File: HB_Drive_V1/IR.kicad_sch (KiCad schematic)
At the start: 55 parts, among them J1 Conn_02x05_Counter_Clockwise, J2 Conn_02x03_Counter_Clockwise, J3 Conn_01x02, U1 TL082, U13 TL082, U2 TL082, U3 TL082, U4 TL082

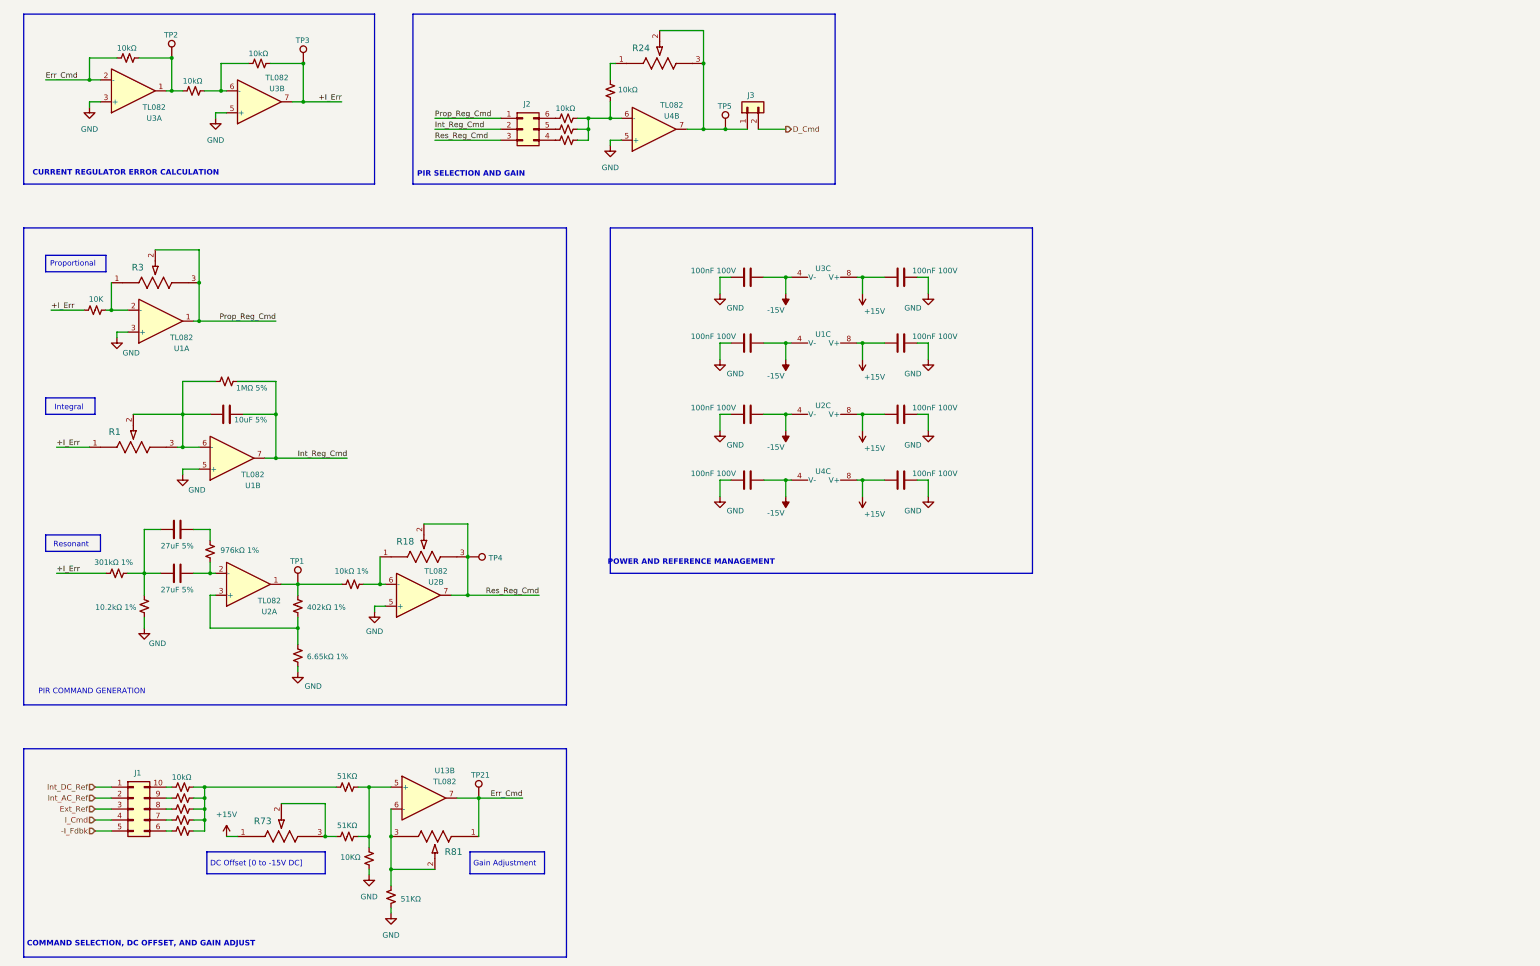
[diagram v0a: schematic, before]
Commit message: finishes hirearchical labels, add 10v +- ref generation and updates the DC offset circuits
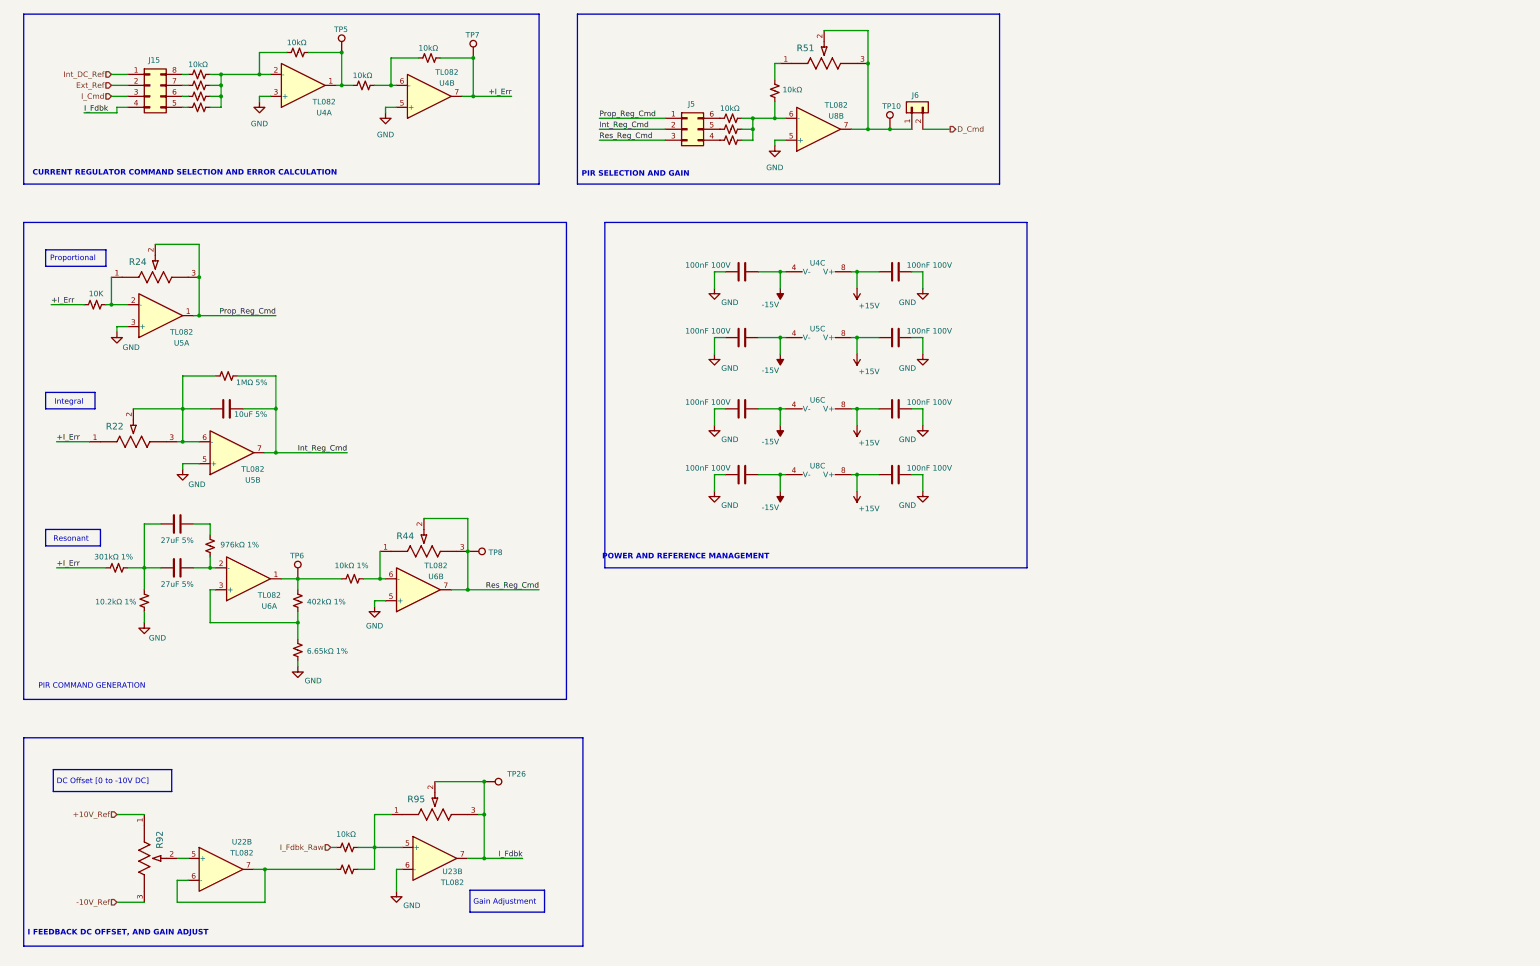
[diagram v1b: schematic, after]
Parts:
- removed J1: Conn_02x05_Counter_Clockwise, Connector_PinHeader_1.27mm:PinHeader_2x05_P1.27mm_Vertical, symbol Connector_Generic:Conn_02x05_Counter_Clockwise
- removed R10, R7, R8, R9: 10K, Resistor_SMD:R_0603_1608Metric_Pad0.98x0.95mm_HandSolder, symbol Device:R_Small_US
- removed R6: 10kΩ, Resistor_SMD:R_0603_1608Metric_Pad0.98x0.95mm_HandSolder, symbol Device:R_Small_US
- removed R73, R81: PV36W104C01B00, PV36W104C01B00:POT_PV36W_BRN, symbol PV36W104C01B00:PV36W104C01B00
- removed R74, R78, R80: 51KΩ, Resistor_SMD:R_0603_1608Metric_Pad0.98x0.95mm_HandSolder, symbol Device:R_Small_US
- removed R79: 10KΩ, Resistor_SMD:R_0603_1608Metric_Pad0.98x0.95mm_HandSolder, symbol Device:R_Small_US
- removed TP21: TestPoint, TestPoint:TestPoint_Loop_D2.60mm_Drill1.6mm_Beaded, symbol Connector:TestPoint
- removed U13: TL082, Package_SO:SOIC-8_5.3x5.3mm_P1.27mm, symbol Amplifier_Operational:TL082
- added J15: Conn_02x04_Counter_Clockwise, Connector_PinSocket_1.27mm:PinSocket_2x04_P1.27mm_Vertical, symbol Connector_Generic:Conn_02x04_Counter_Clockwise
- added R28, R93: 10kΩ, Resistor_SMD:R_0603_1608Metric_Pad0.98x0.95mm_HandSolder, symbol Device:R_Small_US
- added R29, R30, R31: 10K, Resistor_SMD:R_0603_1608Metric_Pad0.98x0.95mm_HandSolder, symbol Device:R_Small_US
- added R92: PV36W104C01B00, PV36W104C01B00:POT_PV36W_BRN, symbol PV36W104C01B00:PV36W104C01B00
- added R94: 10KΩ, Resistor_SMD:R_0603_1608Metric_Pad0.98x0.95mm_HandSolder, symbol Device:R_Small_US
- added R95: PV36W204C01B00, PV36W104C01B00:POT_PV36W_BRN, symbol PV36W104C01B00:PV36W104C01B00
- added TP26: TestPoint, TestPoint:TestPoint_Loop_D2.60mm_Drill1.6mm_Beaded, symbol Connector:TestPoint
- added U22: TL082, Package_SO:SOIC-8_5.3x5.3mm_P1.27mm, symbol Amplifier_Operational:TL082
- added U23: TL082, symbol Amplifier_Operational:TL082
- renumbered C3 to C10, C4 to C11, C5 to C12, C6 to C13, C7 to C14, C8 to C15, C9 to C16, C10 to C17, C11 to C18, C1 to C8, C2 to C9, J2 to J5, J3 to J6, R1 to R22, R2 to R23, R3 to R24, R4 to R25, R13 to R26, R5 to R27, R16 to R33, R11 to R34, R12 to R35, R19 to R37, R14 to R38, R15 to R39, R17 to R42, R18 to R44, R20 to R47, R21 to R48, R22 to R49, R23 to R50, R24 to R51, TP5 to TP10, TP2 to TP5, TP1 to TP6, TP3 to TP7, TP4 to TP8, U3 to U4, U1 to U5, U2 to U6, U4 to U8
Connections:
- net Ext_Ref: now also J15.2 (Pin_2)
- net GND: now also U23.6 (-)
- net I_Cmd: now also J15.3 (Pin_3)
- net Int_DC_Ref: now also J15.1 (Pin_1)
- net Err_Cmd: no longer names the net of R26.2, U4.2 (-)
- net Err_Cmd: now also R28.1, R29.2, R30.2, R31.2
- new net: J15.5 (Pin_5), R31.1
- new net: R93.1, R94.1, R95.1, U23.5 (+)
- new net: J15.8 (Pin_8), R28.2
- new net: J15.7 (Pin_7), R29.1
- new net: J15.6 (Pin_6), R30.1
- new net: R94.2, U22.6 (-), U22.7
- new net: R92.2, U22.5 (+)
- new net +10V_Ref: R92.1
- new net -10V_Ref: R92.3
- new net I_Fdbk: J15.4 (Pin_4), R95.2, R95.3, TP26.1, U23.7
- new net I_Fdbk_Raw: R93.2
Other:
- note added: "CURRENT REGULATOR COMMAND SELECTION AND ERROR CALCULATION"
- note added: "DC Offset [0 to -10V DC]"
- note added: "I FEEDBACK DC OFFSET, AND GAIN ADJUST"
- note removed: "COMMAND SELECTION, DC OFFSET, AND GAIN ADJUST"
- note removed: "CURRENT REGULATOR ERROR CALCULATION"
- note removed: "DC Offset [0 to -15V DC]"
- moved on the sheet: J5, J6, R22, R24, R44, R51, TP10, TP5, TP6, TP7, TP8, U4A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

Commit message: updates board to highest working copy
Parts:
- removed C11, C12, C13, C14, C15, C16, C17, C18: 100nF 100V, Capacitor_SMD:C_0603_1608Metric, symbol Device:C
- removed J15: Conn_02x04_Counter_Clockwise, Connector_PinSocket_1.27mm:PinSocket_2x04_P1.27mm_Vertical, symbol Connector_Generic:Conn_02x04_Counter_Clockwise
- removed J5: Conn_02x03_Counter_Clockwise, Connector_PinSocket_1.27mm:PinSocket_2x03_P1.27mm_Vertical, symbol Connector_Generic:Conn_02x03_Counter_Clockwise
- removed U23: TL082, symbol Amplifier_Operational:TL082
- removed unit 3 of U4
- removed unit 3 of U5
- removed unit 3 of U6
- removed unit 3 of U8
- added C304, C305, C306, C307, C308, C309, C310, C311, C312, C313: 100nF 100V, Capacitor_SMD:C_0603_1608Metric, symbol Device:C
- added J301: Conn_02x03_Odd_Even, Connector_PinHeader_2.54mm:PinHeader_2x03_P2.54mm_Vertical, symbol Connector_Generic:Conn_02x03_Odd_Even
- added J304: Conn_02x04_Odd_Even, Connector_PinHeader_2.54mm:PinHeader_2x04_P2.54mm_Vertical, symbol Connector_Generic:Conn_02x04_Odd_Even
- added R328, R329: 10kΩ, Resistor_SMD:R_0603_1608Metric_Pad0.98x0.95mm_HandSolder, symbol Device:R_Small_US
- added TP307: TestPoint, TestPoint:TestPoint_Loop_D2.60mm_Drill1.6mm_Beaded, symbol Connector:TestPoint
- added unit 2 of U301
- added unit 3 of U301
- added unit 3 of U302
- added unit 3 of U303
- added unit 3 of U304
- added unit 1 of U305
- added unit 3 of U305
- U301: renamed from U22; footprint Package_SO:SOIC-8_5.3x5.3mm_P1.27mm -> Package_SO:SOIC-8_3.9x4.9mm_P1.27mm
- U302: renamed from U4; footprint (none) -> Package_SO:SOIC-8_3.9x4.9mm_P1.27mm
- U303: renamed from U5; footprint Package_SO:SOIC-8_5.3x5.3mm_P1.27mm -> Package_SO:SOIC-8_3.9x4.9mm_P1.27mm
- U304: renamed from U6; footprint (none) -> Package_SO:SOIC-8_3.9x4.9mm_P1.27mm
- U305: renamed from U8; footprint (none) -> Package_SO:SOIC-8_3.9x4.9mm_P1.27mm
- renumbered C8 to C301, C9 to C302, C10 to C303, J6 to J303, R22 to R301, R23 to R302, R24 to R303, R25 to R304, R27 to R305, R92 to R306, R28 to R307, R29 to R308, R30 to R309, R31 to R310, R34 to R311, R35 to R312, R26 to R313, R38 to R314, R39 to R315, R93 to R316, R94 to R317, R42 to R318, R33 to R319, R44 to R320, R95 to R321, R37 to R322, R47 to R323, R48 to R324, R49 to R325, R50 to R326, R51 to R327, TP6 to TP301, TP5 to TP302, TP8 to TP303, TP7 to TP304, TP26 to TP305, TP10 to TP306
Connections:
- net +15V: now also C306.2, C307.2, C310.2, C311.2, C313.2, U301.8 (V+), U302.8 (V+), U303.8 (V+), U304.8 (V+), U305.8 (V+)
- net -15V: now also C304.1, C305.1, C308.1, C309.1, C312.1, U301.4 (V-), U302.4 (V-), U303.4 (V-), U304.4 (V-), U305.4 (V-)
- net GND: now also C304.2, C305.2, C306.1, C307.1, C308.2, C309.2, C310.1, C311.1, C312.2, C313.1, U301.5 (+), U305.3 (+)
- net I_Cmd: now also J304.5 (Pin_5)
- net at R310.1: now also J304.8 (Pin_8)
- net at R316.1, R317.1, R321.1: now also U301.6 (-)
- net at R325.1: now also J301.6 (Pin_6)
- net at R324.1: now also J301.4 (Pin_4)
- net at R323.2: now also J301.2 (Pin_2)
- net at R307.2: now also J304.2 (Pin_2)
- net at R308.1: now also J304.4 (Pin_4)
- net at R309.1: now also J304.6 (Pin_6)
- net at R306.2: now also U301.3 (+); no longer U301.5 (+)
- net I_Fdbk renamed -I_Fdbk
- net -I_Fdbk: now also J304.7 (Pin_7), R328.2, U301.7
- net Int_Reg_Cmd renamed -Int_Reg_Cmd
- net -Int_Reg_Cmd: now also J301.3 (Pin_3)
- net Prop_Reg_Cmd renamed -Prop_Reg_Cmd
- net -Prop_Reg_Cmd: now also J301.1 (Pin_1)
- net Res_Reg_Cmd renamed -Res_Reg_Cmd
- net -Res_Reg_Cmd: now also J301.5 (Pin_5)
- new net: R329.1, TP307.1, U305.1
- new net: R328.1, R329.2, U305.2 (-)
- new net: R317.2, U301.1, U301.2 (-)
- new net Ext_Cmd: J304.3 (Pin_3)
- new net Int_Cmd: J304.1 (Pin_1)
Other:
- note added: "+I_Fdbk"
- moved on the sheet: J303, R301, R303, R306, R320, R321, R327, TP301, TP302, TP303, TP304, TP305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

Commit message: removes Aux file trouble
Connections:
- net -I_Fdbk: no longer R321.2, R321.3, R328.2, TP305.1, U301.7
- new net I_Fdbk: R321.2, R321.3, R328.2, TP305.1, U301.7
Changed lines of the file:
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@@
+	(wire
+		(pts
+			(xy 195.58 43.18) (xy 200.66 43.18)
+		)
+		(stroke
+			(width 0)
+			(type default)
+		)
+	)
 	(wire
 		(pts
@@
 			)
 			(justify left bottom)
-		)
-	)
-	(label "-I_Fdbk"
-		(at 204.47 53.34 180)
-		(effects
-			(font
-				(size 1.27 1.27)
-			)
-			(justify right bottom)
 		)
 	)
@@
 		)
 	)
+	(hierarchical_label "I_Fdbk"
+		(shape output)
+		(at 200.66 43.18 0)
+		(effects
+			(font
+				(size 1.27 1.27)
+			)
+			(justify left)
+		)
+	)
